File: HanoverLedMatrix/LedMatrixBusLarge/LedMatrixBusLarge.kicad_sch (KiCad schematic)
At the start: 22 parts

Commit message: feat: Updated the symbol of 74HC373D
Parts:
- C12, C13: value (none) -> C_Small
- D1, D? (x3): value (none) -> D_Small
- J1: value (none) -> Conn1
- J2: value (none) -> Conn2
- J?: value (none) -> Conn_ID_selector
- R13: value (none) -> 10K
- R14: value (none) -> 10k
- R6: value (none) -> 2K7
- R7: value (none) -> 1K3
- U1, U2: value (none) -> 74HC138D-T; footprint (none) -> SOIC127P600X175-16N
- U10, U5, U7, U9: value (none) -> 74HC373D; footprint (none) -> SOIC127P1032X265-20N
- U4: value (none) -> 74HC14D,652; footprint (none) -> SOIC127P600X175-14N
- U6, U8: value (none) -> 74HC164
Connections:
- net PullUpR: no longer R13.2, U1.4 (~{E1})
- new net: R13.2, U1.4 (~{E1})
- no-connect marks 20 -> 25
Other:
- note removed: "R13"
- moved on the sheet: R13, U10, U5, U7, U8, U9

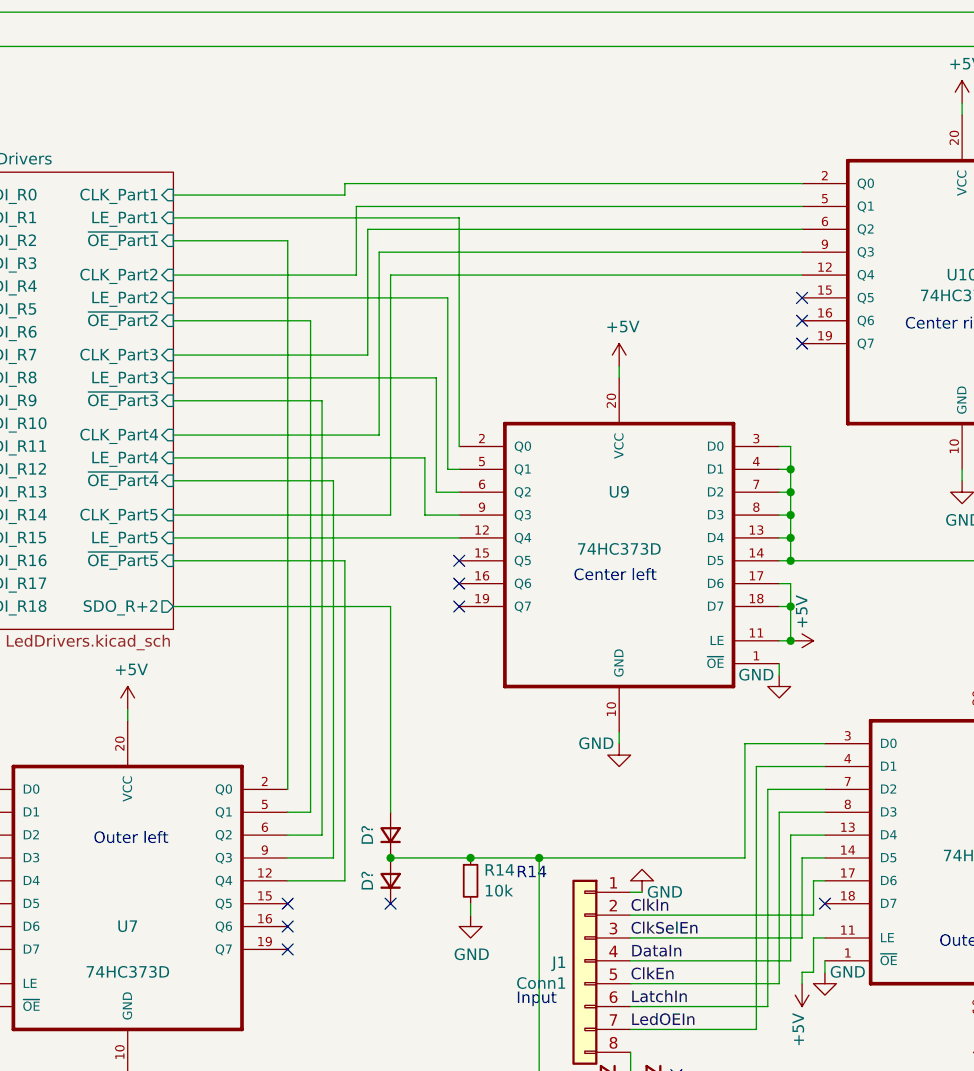
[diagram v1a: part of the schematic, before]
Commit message: feat: using label for the connections to the LED drivers
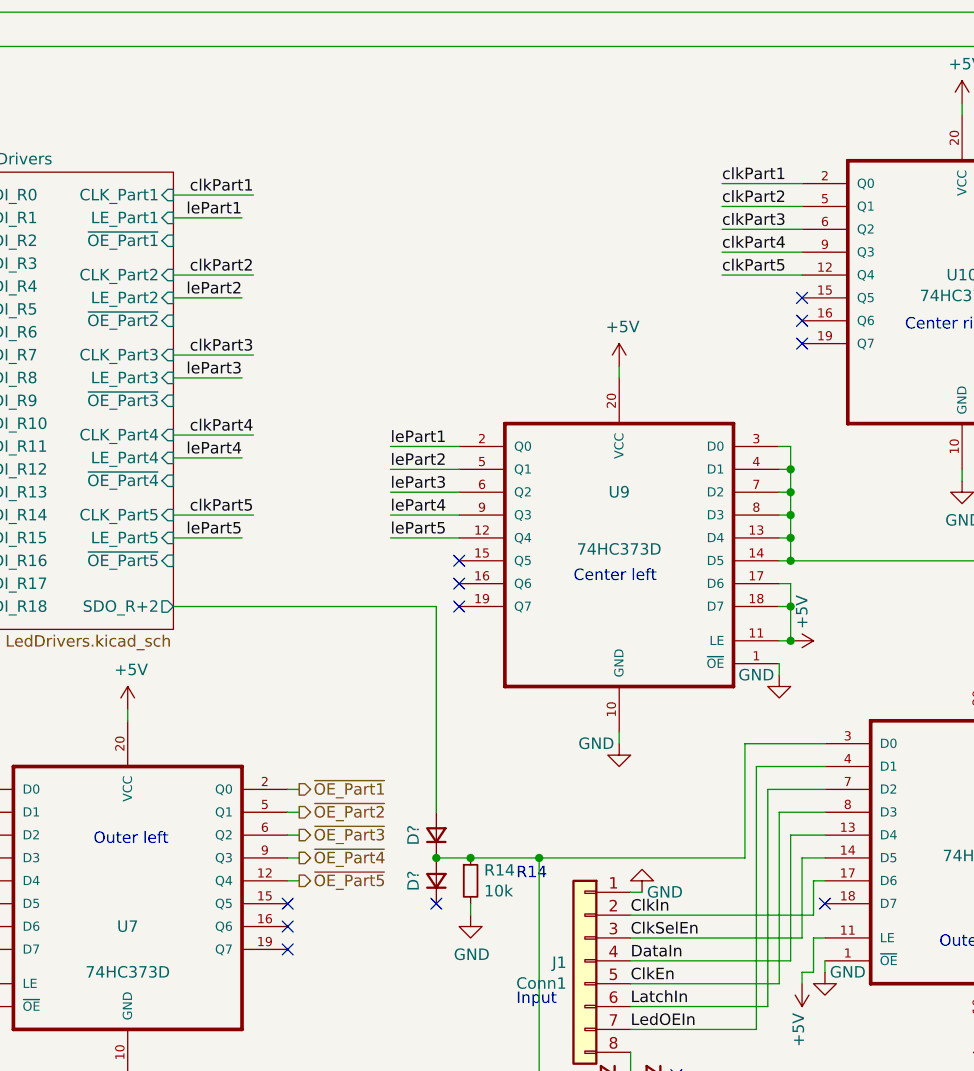
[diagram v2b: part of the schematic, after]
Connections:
- net LedDrivers/~{OE_Part1}: no longer U7.2 (Q0)
- net LedDrivers/~{OE_Part2}: no longer U7.5 (Q1)
- net LedDrivers/~{OE_Part3}: no longer U7.6 (Q2)
- net LedDrivers/~{OE_Part4}: no longer U7.9 (Q3)
- net LedDrivers/~{OE_Part5}: no longer U7.12 (Q4)
- net LedDrivers/CLK_Part1 renamed clkPart1
- net LedDrivers/CLK_Part2 renamed clkPart2
- net LedDrivers/CLK_Part3 renamed clkPart3
- net LedDrivers/CLK_Part4 renamed clkPart4
- net LedDrivers/CLK_Part5 renamed clkPart5
- net LedDrivers/LE_Part1 renamed lePart1
- net LedDrivers/LE_Part2 renamed lePart2
- net LedDrivers/LE_Part3 renamed lePart3
- net LedDrivers/LE_Part4 renamed lePart4
- net LedDrivers/LE_Part5 renamed lePart5
- new net ~{OE_Part1}: U7.2 (Q0)
- new net ~{OE_Part2}: U7.5 (Q1)
- new net ~{OE_Part3}: U7.6 (Q2)
- new net ~{OE_Part4}: U7.9 (Q3)
- new net ~{OE_Part5}: U7.12 (Q4)
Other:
- moved on the sheet: D?

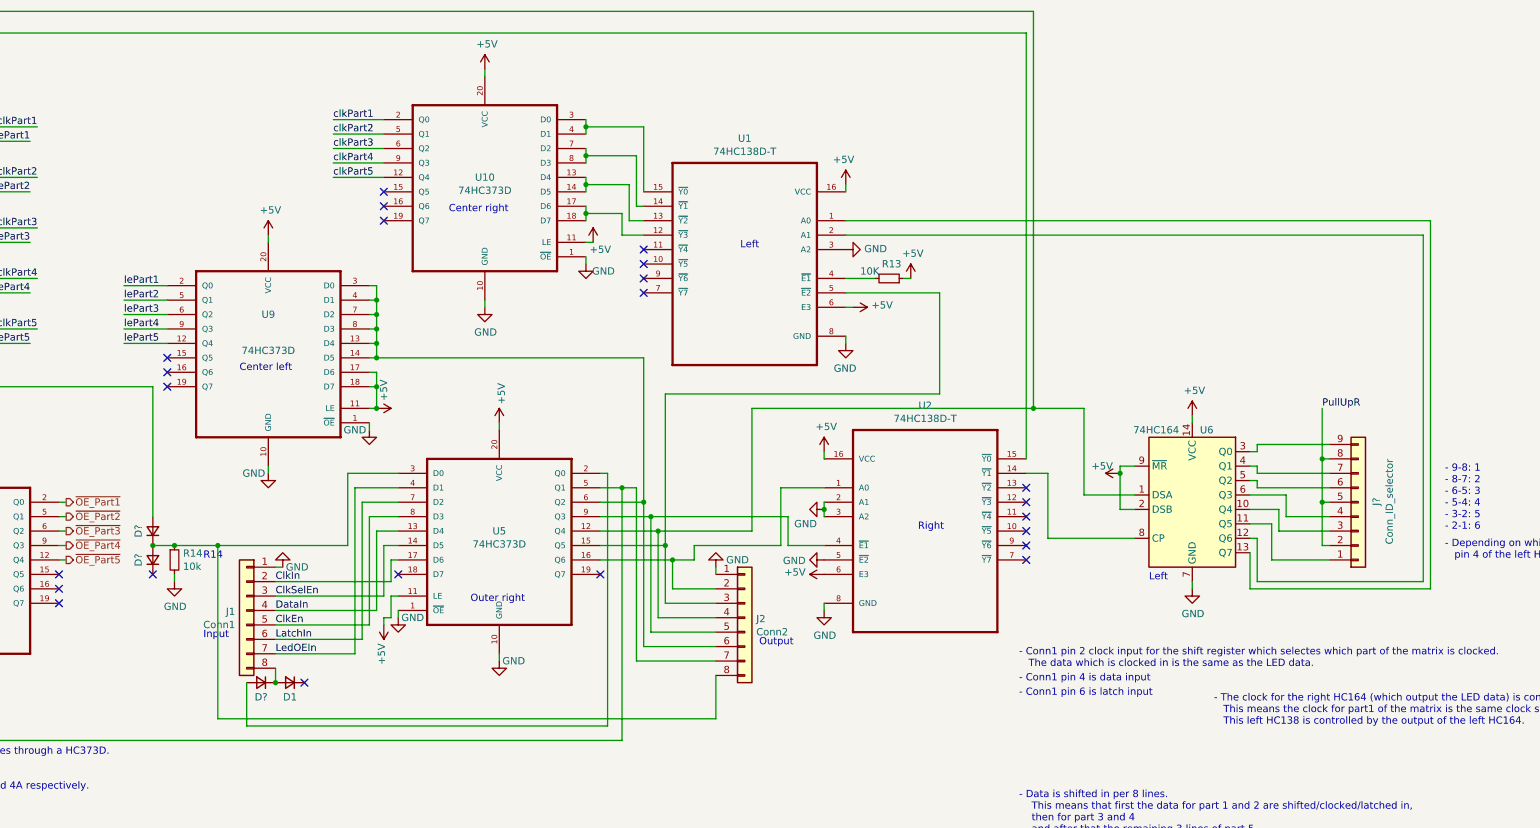
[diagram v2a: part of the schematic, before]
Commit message: feat: updated symbol of 74HC138D-T
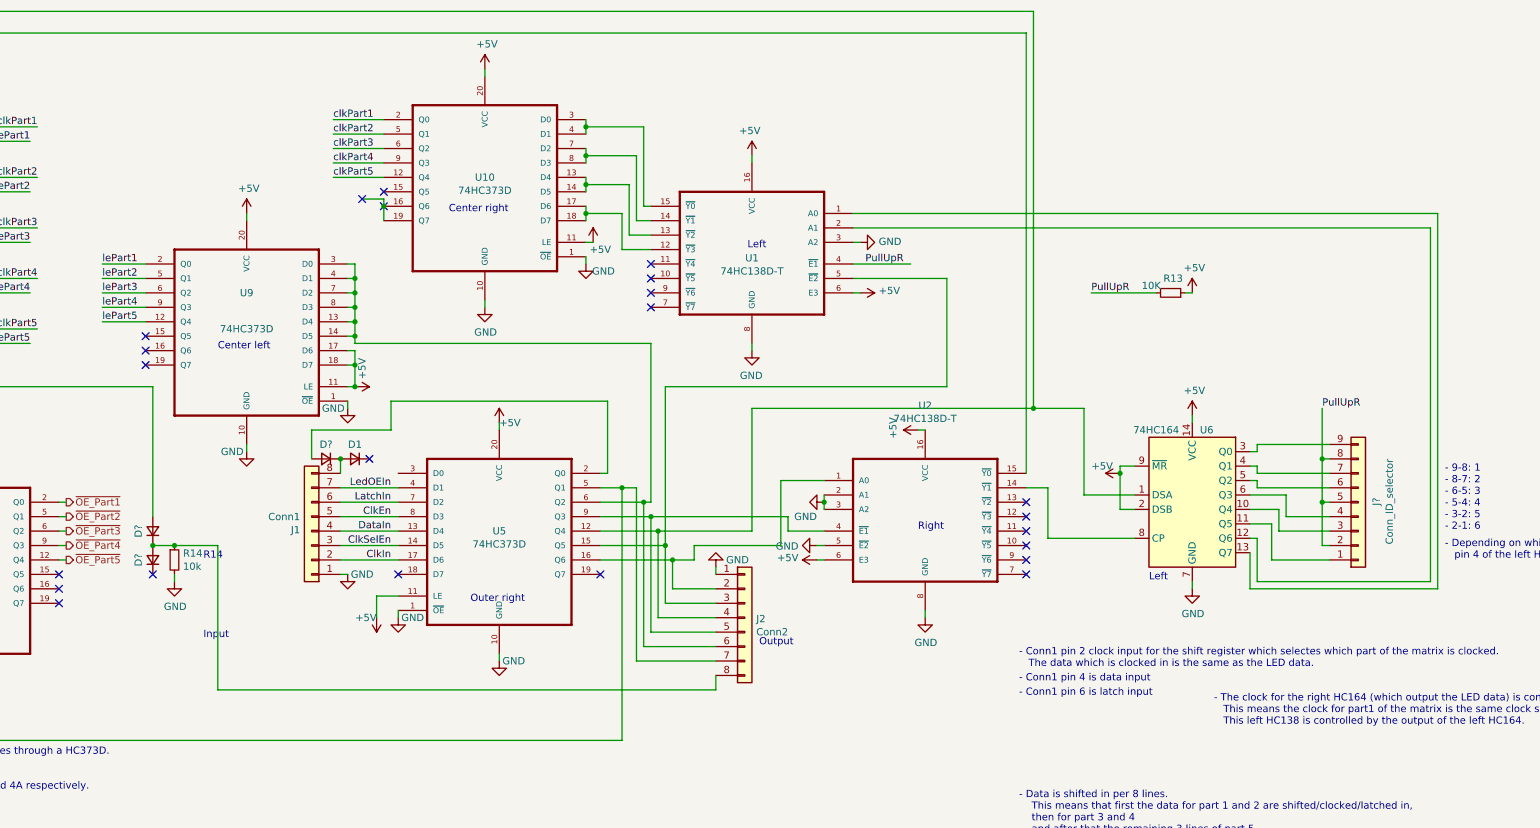
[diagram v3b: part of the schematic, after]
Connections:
- net PullUpR: now also R13.2, U1.4 (~{E1})
- net at D?.1 (K), D?.2 (A), J2.8 (Pin_8)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: no longer U5.3 (D0)
- net at U10.16 (Q6): now also U10.19 (Q7)
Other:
- moved on the sheet: D1, D?, J1, R13, U1, U2, U9

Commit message: feat: made everything fit into the allocated space
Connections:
- net dataIn: now reaches J2.4 (Pin_4), U5.12 (Q4), U6.1 (DSA), U8.1 (DSA)
- net clkSectionClk74HC164: now reaches U2.14 (~{Y1}), U6.8 (CP)
- net clkLed74HC164: now reaches U2.15 (~{Y0}), U8.8 (CP)
- net clkIn: now reaches J2.2 (Pin_2), U2.1 (A0), U5.16 (Q6)
- net clkEn: now reaches J2.5 (Pin_5), U2.4 (~{E1}), U5.9 (Q3)
- net clkSelEn: now reaches J2.3 (Pin_3), U1.5 (~{E2}), U5.15 (Q5)
- net ledOEIn: now reaches J2.7 (Pin_7), U4.1 (1A), U4.3 (2A), U5.5 (Q1), U7.3 (D0), U7.4 (D1)
- net latchIn: now reaches J2.6 (Pin_6), U5.6 (Q2), U9.13 (D4), U9.14 (D5), U9.3 (D0), U9.4 (D1), U9.7 (D2), U9.8 (D3)
- net at U10.16 (Q6): no longer U10.19 (Q7)
- net SDO_R+2 filtered: now reaches D?.1 (K), D?.2 (A), J2.8 (Pin_8), R14.1
- net ClkEn renamed _clkEn_
- net ClkIn renamed _clkIn_
- net ClkSelEn renamed _clkSelEn_
- net DataIn renamed _dataIn_
- net LatchIn renamed _latchIn_
- net LedOEIn renamed _ledOEIn_
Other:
- note removed: "R14"
- note removed: "R6"
- note removed: "R7"
- moved on the sheet: C12, C13, D1, D?, J1, J2, J?, R13, R14, R6, R7, U1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

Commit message: wip: cleanup
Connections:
- net GND: now also C12.1, C13.1; no longer C12.2, C13.2
- net clkPartSel1: now reaches U1.2 (A1), U6.12 (Q6)
- net clkPartSel0: now reaches U1.1 (A0), U6.13 (Q7)
- net at U4.2 (1Y): now also R7.1; no longer R7.2
- net at R6.2, U4.9 (4A): now also C13.2; no longer C13.1
- net LedDrivers/SDI_R0 renamed ledData7
- net LedDrivers/SDI_R1 renamed ledData6
- net LedDrivers/SDI_R10 renamed ledData5
- net LedDrivers/SDI_R11 renamed ledData4
- net LedDrivers/SDI_R12 renamed ledData3
- net LedDrivers/SDI_R13 renamed ledData2
- net LedDrivers/SDI_R14 renamed ledData1
- net LedDrivers/SDI_R15 renamed ledData0
- new net: C12.2, R7.2, U4.5 (3A)
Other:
- note removed: "- Conn1 pin 4 is data input"
- note removed: "- Conn1 pin 6 is latch input"
- note removed: "C12"
- moved on the sheet: C12, C13, D?, J2, R13, R14, R6, R7, U1, U10, U2, U7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

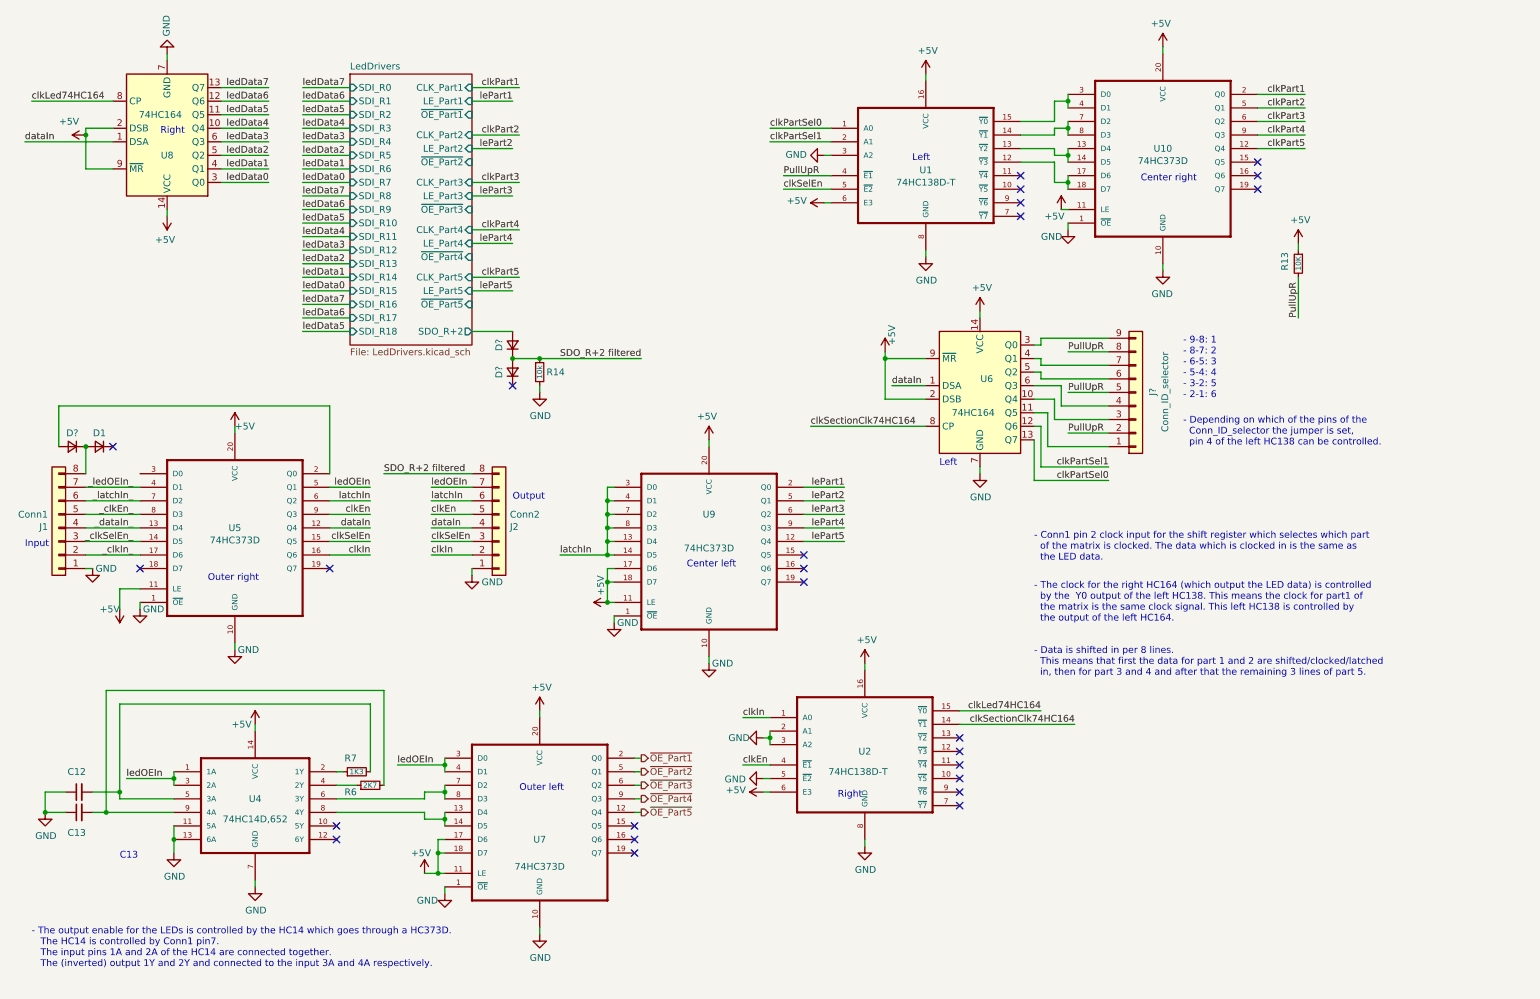
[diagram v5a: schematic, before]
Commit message: feat: organised the schematic into blocks and updated the readme
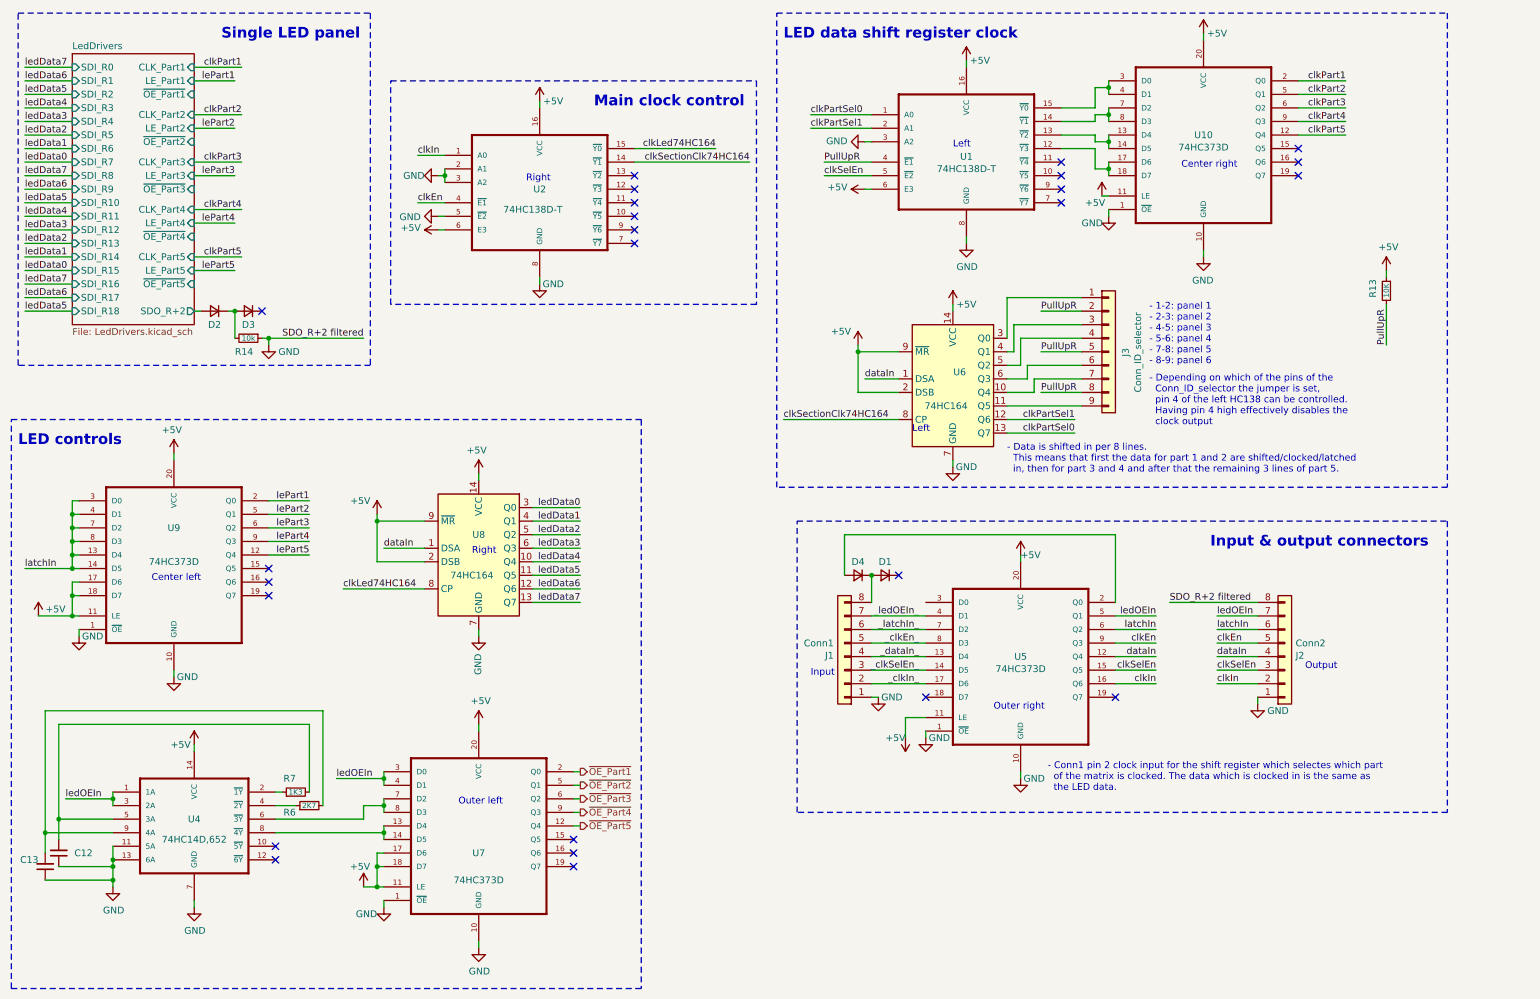
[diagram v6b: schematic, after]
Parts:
- gave numbers to parts that had none: 4
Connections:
- net GND: now also J2.8 (Pin_8), R14.1; no longer R14.2
- net at U6.10 (Q4): now also J3.7 (Pin_7); no longer J3.3 (Pin_3)
- net at U6.11 (Q5): now also J3.9 (Pin_9); no longer J3.1 (Pin_1)
- net at U6.3 (Q0): now also J3.1 (Pin_1); no longer J3.9 (Pin_9)
- net at U6.4 (Q1): now also J3.3 (Pin_3); no longer J3.7 (Pin_7)
- net at U6.5 (Q2): now also J3.4 (Pin_4); no longer J3.6 (Pin_6)
- net at U6.6 (Q3): now also J3.6 (Pin_6); no longer J3.4 (Pin_4)
- net SDO_R+2 filtered: no longer names the net of D2.1 (K), D3.2 (A)
- net SDO_R+2 filtered: now also R14.2; no longer J2.8 (Pin_8), R14.1
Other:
- note added: "- 1-2: panel 1 - 2-3: panel 2 - 4-5: panel 3 - 5-6: panel 4 - 7-8: panel 5 - 8-9: panel 6"
- note added: "- Depending on which of the pins of the Conn_ID_selector the jumper is set, pin 4 of the left HC138 can be controlled. Having pin 4 high effectively disables the clock output"
- note added: "Input & output connectors"
- note added: "LED controls"
- note added: "LED data shift register clock"
- note added: "Main clock control"
- note added: "Single LED panel"
- note removed: "- 9-8: 1 - 8-7: 2 - 6-5: 3 - 5-4: 4 - 3-2: 5 - 2-1: 6"
- note removed: "- Depending on which of the pins of the Conn_ID_selector the jumper is set, pin 4 of the left HC138 can be controlled."
- note removed: "- The clock for the right HC164 (which output the LED data) is controlled by the Y0 output of the left HC138. This means the clock for part1 of the matrix is the same clock signal. This left HC138 is controlled by the output of the left HC164."
- note removed: "- The output enable for the LEDs is controlled by the HC14 which goes through a HC373D. The HC14 is controlled by Conn1 pin7. The input pins 1A and 2A of the HC14 are connected together. The (inverted) output 1Y and 2Y and connected to the input 3A and 4A respectively."
- note removed: "C13"
- moved on the sheet: C12, C13, D1, D2, D3, D4, J1, J2, J3, R13, R14, R6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
